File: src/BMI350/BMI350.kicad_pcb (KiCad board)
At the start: 2 copper layers, 5 parts, among them U1 STM32H750VBTx, U2 BMM350

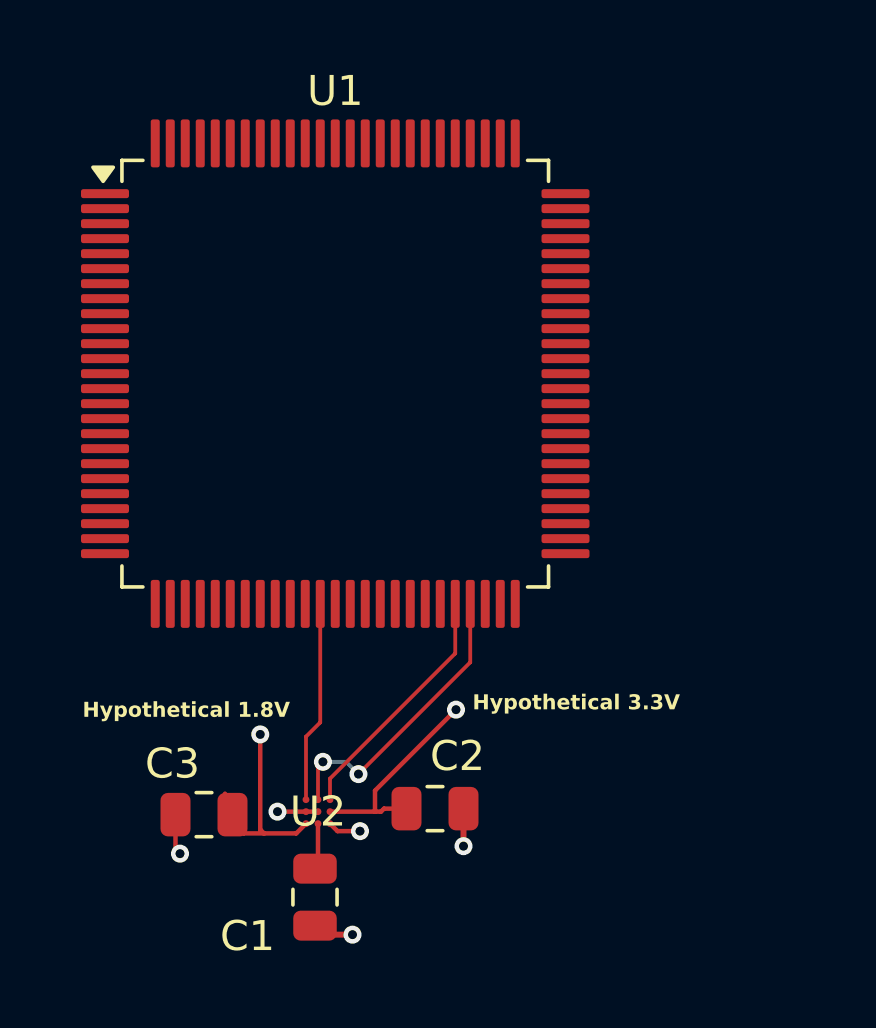
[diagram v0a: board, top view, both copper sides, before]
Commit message: Voltage Divider
Added voltage divider for BMM350 1.8V power supply
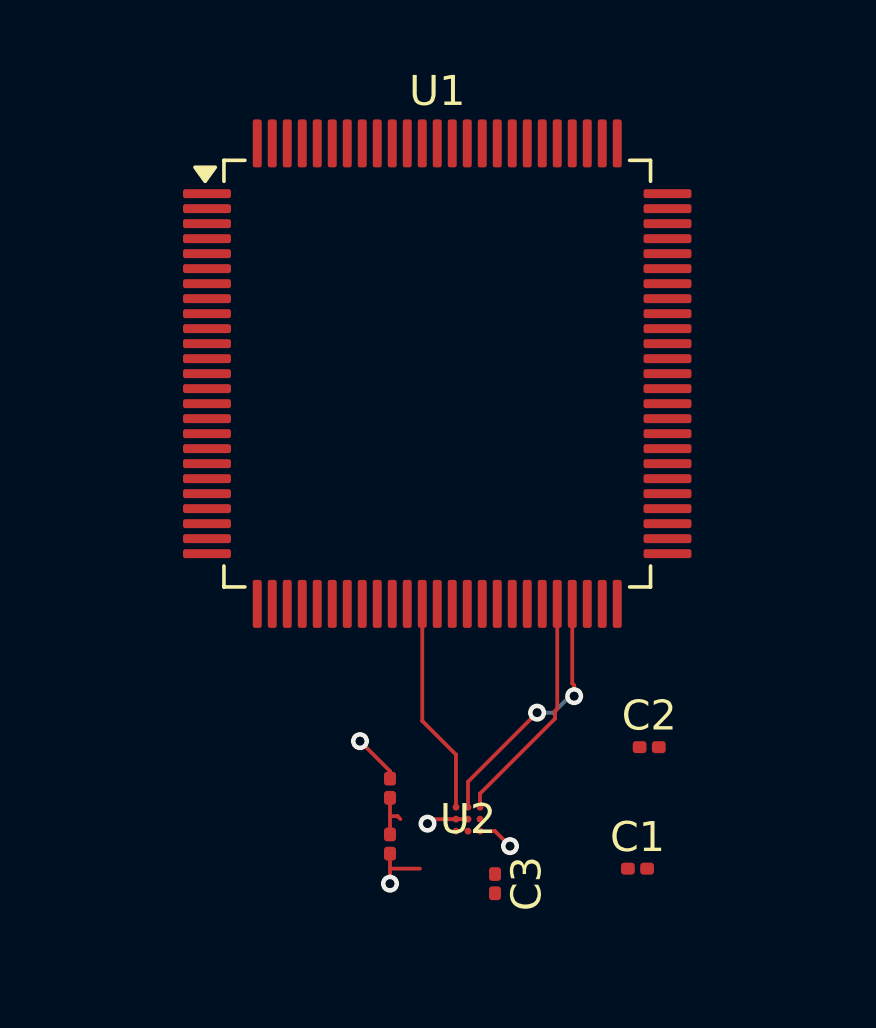
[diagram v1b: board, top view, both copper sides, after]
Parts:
- added R1: 1kOhm, Resistor_SMD:R_0201_0603Metric, F.Cu at (138.0, 114.8)
- added R2: 1kOhm, Resistor_SMD:R_0201_0603Metric, F.Cu at (138.0, 116.7)
- C1: value 2.2uF -> 100nF; footprint Capacitor_SMD:C_0805_2012Metric -> Capacitor_SMD:C_0201_0603Metric
- C2: value 100nF -> 2.2uF; footprint Capacitor_SMD:C_0805_2012Metric -> Capacitor_SMD:C_0201_0603Metric
- C3: footprint Capacitor_SMD:C_0805_2012Metric -> Capacitor_SMD:C_0201_0603Metric
- U2: footprint BMM350 Footprints:BGA9_BMM350_BOS -> BMM350 Footprints2:BGA9_BMM350_BOS
- moved C1 10.8 mm to (146.2, 117.5), turned to 0 degrees
- moved C3 9.97 mm to (141.5, 118.0), turned to -90 degrees
- moved C2 7.43 mm to (146.6, 113.5)
- moved U2 5.01 mm to (140.6, 115.8)
- moved U1 3.40 mm to (139.6, 101.0)
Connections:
- C1 pad 1: GND -> +1V8
- C1 pad 2: GND -> +1V8
- C2 pad 1: +3.3V -> +1V8
- C2 pad 2: GND -> +1V8
- C3 pad 1: GND -> +3.3V
- U2 pad B1: GND -> +1V8
- U2 pad B2: GND -> +1V8
- U2 pad C2: GND -> +1V8
- U2 pad C3: GND -> +1V8
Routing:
- net GND: track 7.92 -> 0.00 mm, vias 5 -> 0
- net +3.3V: track 7.11 -> 1.66 mm
- net I2C_SDA: track 9.90 -> 8.67 mm
- net +1V8: track 7.18 -> 6.23 mm, vias 1 -> 3
- net GPIO_EXTI: track 6.72 -> 7.24 mm
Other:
- board text removed: "Hypothetical 1.8V"
- board text removed: "Hypothetical 3.3V"

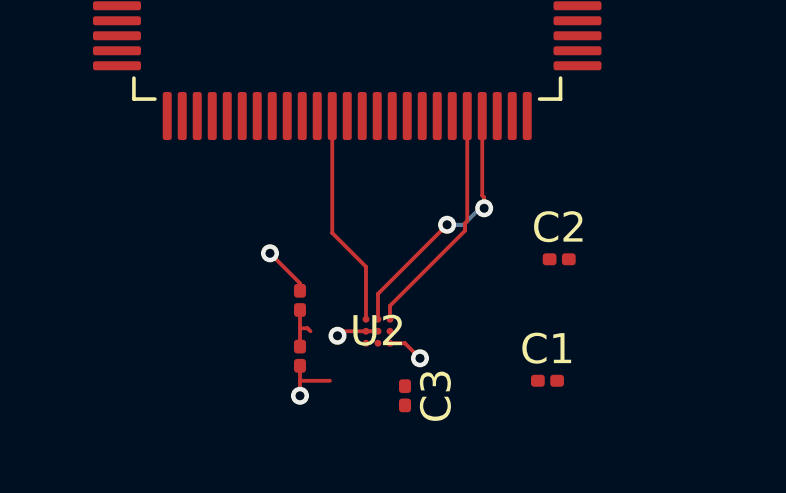
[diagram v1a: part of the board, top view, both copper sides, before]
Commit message: BMM forgot
Forgot to save files before pushing
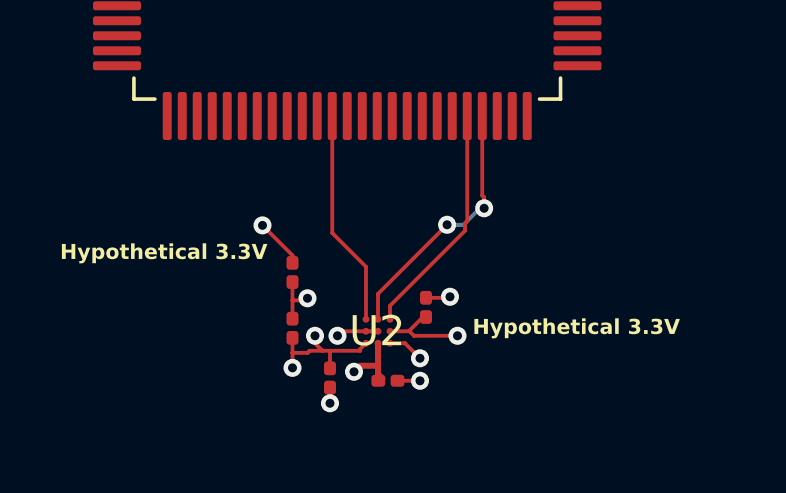
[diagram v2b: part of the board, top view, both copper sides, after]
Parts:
- moved C1 7.25 mm to (139.0, 117.4), turned to 90 degrees
- moved C2 7.00 mm to (140.9, 117.5), turned to 180 degrees
- moved C3 3.03 mm to (142.2, 115.1), turned to 90 degrees
- moved R2 0.96 mm to (137.8, 115.8)
- moved R1 0.96 mm to (137.8, 113.9)
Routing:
- net +1V8: track 6.23 -> 13.5 mm, vias 3 -> 9
- net +3.3V: track 1.66 -> 4.64 mm, vias 1 -> 2
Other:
- board text added: "Hypothetical 3.3V"

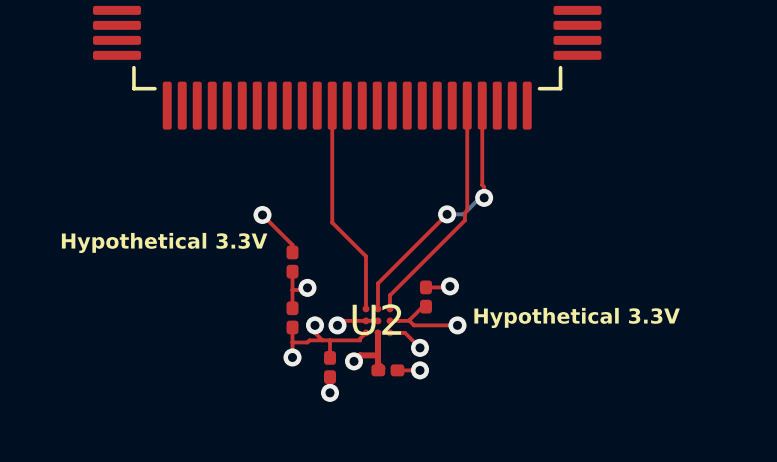
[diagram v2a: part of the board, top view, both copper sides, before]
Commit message: Voltage Divider
Fixed voltage divider outputs
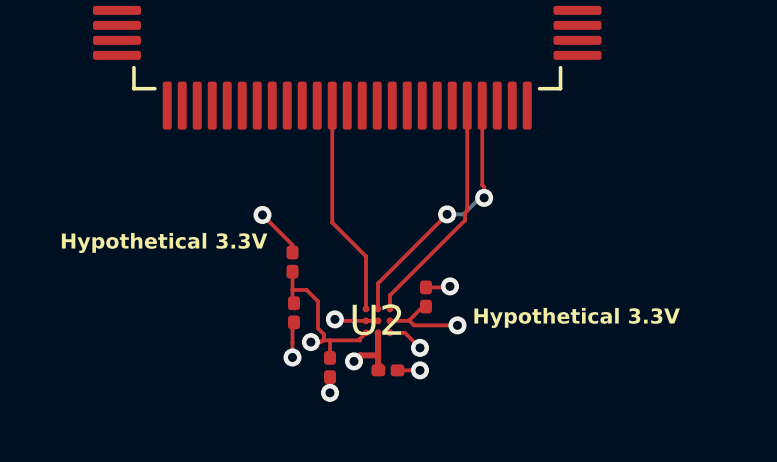
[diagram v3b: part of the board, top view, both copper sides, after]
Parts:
- moved R2 0.18 mm to (137.8, 115.6), turned to -90 degrees
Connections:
- C1 pad 1: +1V8 -> GND
- C2 pad 1: +1V8 -> GND
- C2 pad 2: +1V8 -> GND
- C3 pad 2: +1V8 -> GND
- R2 pad 2: +1V8 -> GND
- U2 pad B1: +1V8 -> GND
- U2 pad B2: +1V8 -> GND
- U2 pad C2: +1V8 -> GND
- U2 pad C3: +1V8 -> GND
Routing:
- net GND: track 0.00 -> 7.98 mm, vias 0 -> 7
- net +1V8: track 13.5 -> 6.19 mm, vias 9 -> 1

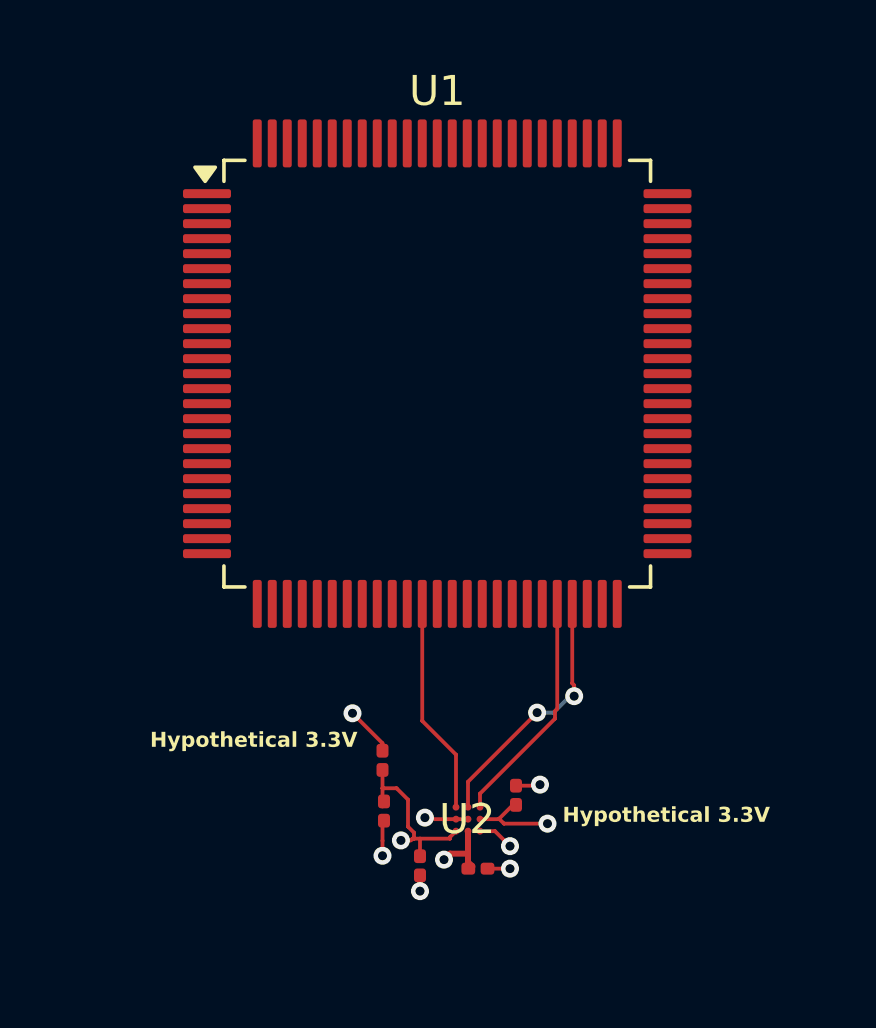
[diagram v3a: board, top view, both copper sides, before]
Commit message: Buck Converter
Redid BM350 breakout schematic with 3.3-1.8 buck converter instead of voltage divider
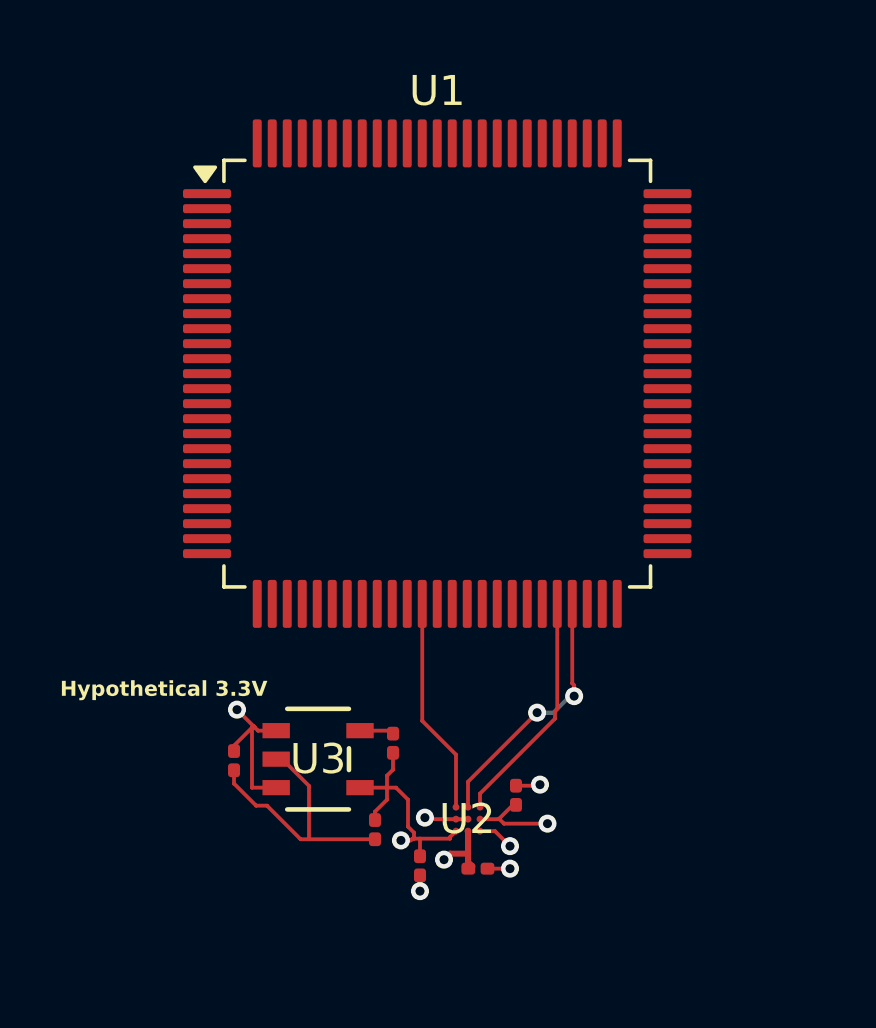
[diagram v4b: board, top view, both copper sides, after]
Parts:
- removed R1, R2: 1kOhm, Resistor_SMD:R_0201_0603Metric
- added C4: 10uF, Capacitor_SMD:C_0201_0603Metric, F.Cu at (132.8, 113.9)
- added C5: 22uF, Capacitor_SMD:C_0201_0603Metric, F.Cu at (137.5, 116.2)
- added L1: 10uH, Inductor_SMD:L_0201_0603Metric, F.Cu at (138.1, 113.3)
- added U3: XC9265C181MR-G, XC9529:SOT_181MR-G_TOR, F.Cu at (135.6, 113.9)
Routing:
- net GND: track 7.98 -> 16.1 mm, vias 7 -> 6
- net +3.3V: track 4.64 -> 8.47 mm
- net +1V8: track 6.19 -> 8.21 mm
- net Net-(U3-LX): track 0.00 -> 1.14 mm

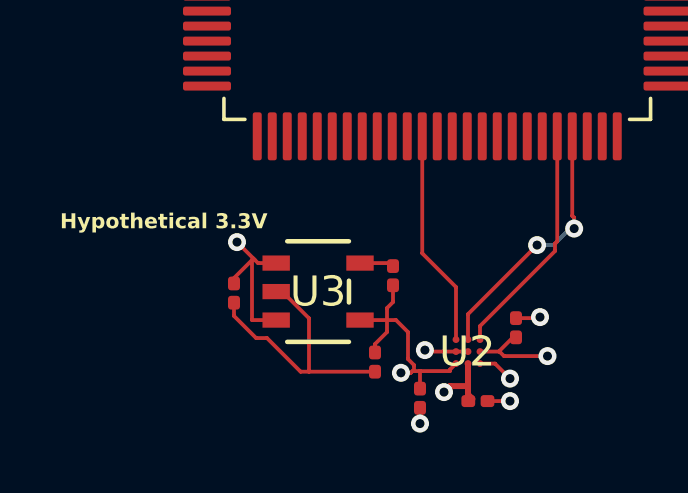
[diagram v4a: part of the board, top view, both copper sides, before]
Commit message: S-85S1A
Added S-85S1A to flight computer schematic
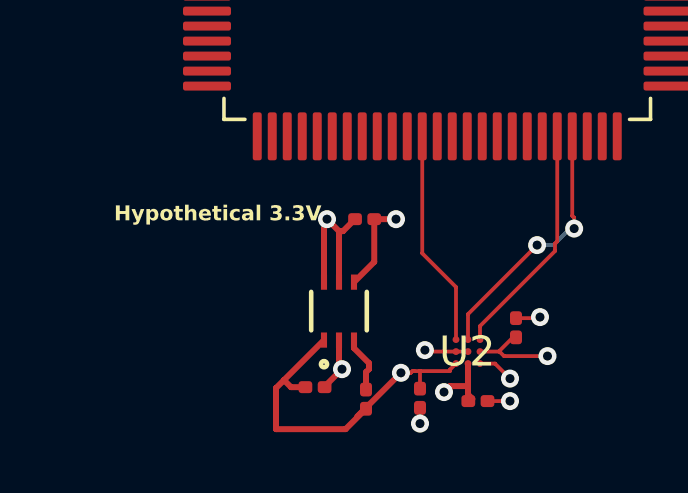
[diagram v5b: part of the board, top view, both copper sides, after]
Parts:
- C5: value 22uF -> 10uF
- L1: value 10uH -> 2.2uH
- U3: value XC9265C181MR-G -> S-85S1AB33-I6T1U; footprint XC9529:SOT_181MR-G_TOR -> footprints:SNT-6A-A-PKG_PG006-A-P-SD-2.1_ABL
- moved C5 4.78 mm to (137.2, 111.4), turned to 0 degrees
- moved L1 4.21 mm to (137.2, 117.4)
- moved C4 4.14 mm to (135.5, 117.0), turned to 180 degrees
- moved U3 0.95 mm to (136.3, 114.5), turned to 90 degrees
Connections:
- C4 pad 1: +3.3V -> Earth
- C4 pad 2: GND -> +1V8
- C5 pad 1: GND -> +3.3V
- C5 pad 2: +1V8 -> Earth
- L1 pad 1: Net-(U3-LX) -> Net-(U3-SW)
- U3 pad 1: +3.3V -> +1V8
- U3 pad 2: GND -> Earth
- U3 pad 3: +3.3V -> Net-(U3-SW)
- U3 pad 4: +1V8 -> Earth
- U3 pad 5: Net-(U3-LX) -> +3.3V
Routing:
- net GND: track 16.1 -> 6.98 mm
- net Earth: track 0.00 -> 4.96 mm, vias 0 -> 2
- net +1V8: track 8.21 -> 12.4 mm
- net Net-(U3-SW): track 0.00 -> 1.90 mm
- net Net-(U3-LX): track 1.14 -> 0.00 mm
